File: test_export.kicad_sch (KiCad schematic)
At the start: 2 parts, among them U1 TestMCU

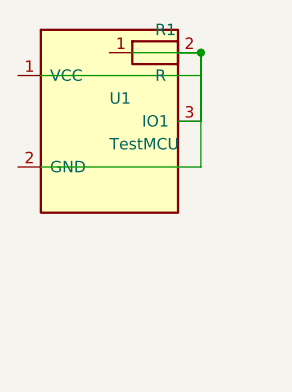
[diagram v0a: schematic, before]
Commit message: Fix duplicate reference designators, false positive PCB DRC clearance violations, and restore trace overlap resolution
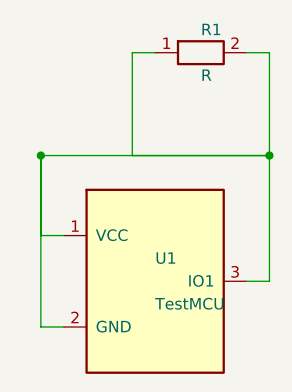
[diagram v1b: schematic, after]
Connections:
- net at R1.1: now also R1.2, U1.1 (VCC), U1.2 (GND), U1.3 (IO1)
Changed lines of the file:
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@@
 (kicad_sch (version 20231120) (generator "circuitbot") (generator_version "1.0")
   (paper "A3")
-  (symbol (lib_id "MCU_Module:TestMCU") (at 58.42 58.42 0) (unit 1)
+  (symbol (lib_id "MCU_Module:TestMCU") (at 63.5 76.2 0) (unit 1)
     (in_bom yes) (on_board yes) (dnp no)
-    (property "Reference" "U1" (at 58.42 55.88 0)
+    (property "Reference" "U1" (at 63.5 73.66 0)
       (effects (font (size 1.27 1.27)) (justify left))
     )
-    (property "Value" "TestMCU" (at 58.42 60.96 0)
+    (property "Value" "TestMCU" (at 63.5 78.74 0)
       (effects (font (size 1.27 1.27)) (justify left))
     )
-    (property "Footprint" "" (at 58.42 58.42 0)
+    (property "Footprint" "" (at 63.5 76.2 0)
       (effects (font (size 1.27 1.27)) hide)
     )
-    (property "Datasheet" "" (at 58.42 58.42 0)
+    (property "Datasheet" "" (at 63.5 76.2 0)
       (effects (font (size 1.27 1.27)) hide)
     )
@@
     (instances
       (project "circuitbot"
-        (path "/c2199af7-c479-45ad-89b1-c0f63471e519" (reference "U1") (unit 1))
+        (path "/90fcbd86-16bf-4343-8192-f2305b034c51" (reference "U1") (unit 1))
       )
     )
   )
-  (symbol (lib_id "Device:R") (at 63.5 50.8 0) (unit 1)
+  (symbol (lib_id "Device:R") (at 68.58 50.8 0) (unit 1)
     (in_bom yes) (on_board yes) (dnp no)
-    (property "Reference" "R1" (at 63.5 48.26 0)
+    (property "Reference" "R1" (at 68.58 48.26 0)
       (effects (font (size 1.27 1.27)) (justify left))
     )
-    (property "Value" "R" (at 63.5 53.34 0)
+    (property "Value" "R" (at 68.58 53.34 0)
       (effects (font (size 1.27 1.27)) (justify left))
     )
-    (property "Footprint" "" (at 63.5 50.8 0)
+    (property "Footprint" "" (at 68.58 50.8 0)
       (effects (font (size 1.27 1.27)) hide)
     )
-    (property "Datasheet" "" (at 63.5 50.8 0)
+    (property "Datasheet" "" (at 68.58 50.8 0)
       (effects (font (size 1.27 1.27)) hide)
     )
@@
     (instances
       (project "circuitbot"
-        (path "/c2199af7-c479-45ad-89b1-c0f63471e519" (reference "R1") (unit 1))
+        (path "/90fcbd86-16bf-4343-8192-f2305b034c51" (reference "R1") (unit 1))
       )
     )
   )
-  (wire (pts (xy 66.04 58.42) (xy 68.58 58.42))
+  (wire (pts (xy 73.66 76.2) (xy 76.2 76.2))
     (stroke (width 0) (type default))
   )
-  (wire (pts (xy 68.58 58.42) (xy 68.58 50.8))
+  (wire (pts (xy 76.2 76.2) (xy 76.2 62.23))
     (stroke (width 0) (type default))
   )
-  (wire (pts (xy 68.58 50.8) (xy 60.96 50.8))
+  (wire (pts (xy 76.2 62.23) (xy 60.96 62.23))
     (stroke (width 0) (type default))
   )
-  (wire (pts (xy 50.8 53.34) (xy 68.58 53.34))
+  (wire (pts (xy 60.96 62.23) (xy 60.96 50.8))
     (stroke (width 0) (type default))
   )
-  (wire (pts (xy 68.58 53.34) (xy 68.58 50.8))
+  (wire (pts (xy 60.96 50.8) (xy 63.5 50.8))
     (stroke (width 0) (type default))
   )
-  (wire (pts (xy 68.58 50.8) (xy 66.04 50.8))
+  (wire (pts (xy 53.34 71.12) (xy 50.8 71.12))
     (stroke (width 0) (type default))
   )
-  (wire (pts (xy 50.8 63.5) (xy 68.58 63.5))
+  (wire (pts (xy 50.8 71.12) (xy 50.8 62.23))
     (stroke (width 0) (type default))
   )
-  (wire (pts (xy 68.58 63.5) (xy 68.58 50.8))
+  (wire (pts (xy 50.8 62.23) (xy 76.2 62.23))
     (stroke (width 0) (type default))
   )
-  (junction (at 68.58 50.8) (diameter 0) (color 0 0 0 0)
+  (wire (pts (xy 76.2 62.23) (xy 76.2 50.8))
+    (stroke (width 0) (type default))
+  )
+  (wire (pts (xy 76.2 50.8) (xy 73.66 50.8))
+    (stroke (width 0) (type default))
+  )
+  (wire (pts (xy 53.34 81.28) (xy 50.8 81.28))
+    (stroke (width 0) (type default))
+  )
+  (wire (pts (xy 50.8 81.28) (xy 50.8 62.23))
+    (stroke (width 0) (type default))
+  )
+  (junction (at 76.2 62.23) (diameter 0) (color 0 0 0 0)
+  )
+  (junction (at 50.8 62.23) (diameter 0) (color 0 0 0 0)
   )
   (sheet_instances (path "/" (page "1")))

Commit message: Feat : Optimized the reRouting
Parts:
- removed R1: R, symbol Device:R
- removed U1: TestMCU, symbol MCU_Module:TestMCU
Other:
- title: (none) -> Smart USB Thumb Drive
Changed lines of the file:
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@@
 (kicad_sch (version 20231120) (generator "circuitbot") (generator_version "1.0")
   (paper "A3")
-  (symbol (lib_id "MCU_Module:TestMCU") (at 63.5 76.2 0) (unit 1)
-    (in_bom yes) (on_board yes) (dnp no)
-    (property "Reference" "U1" (at 63.5 73.66 0)
-      (effects (font (size 1.27 1.27)) (justify left))
-    )
-    (property "Value" "TestMCU" (at 63.5 78.74 0)
-      (effects (font (size 1.27 1.27)) (justify left))
-    )
-    (property "Footprint" "" (at 63.5 76.2 0)
-      (effects (font (size 1.27 1.27)) hide)
-    )
-    (property "Datasheet" "" (at 63.5 76.2 0)
-      (effects (font (size 1.27 1.27)) hide)
-    )
-    (pin "1")
-    (pin "2")
-    (pin "3")
-    (instances
-      (project "circuitbot"
-        (path "/90fcbd86-16bf-4343-8192-f2305b034c51" (reference "U1") (unit 1))
-      )
-    )
-  )
-  (symbol (lib_id "Device:R") (at 68.58 50.8 0) (unit 1)
-    (in_bom yes) (on_board yes) (dnp no)
-    (property "Reference" "R1" (at 68.58 48.26 0)
-      (effects (font (size 1.27 1.27)) (justify left))
-    )
-    (property "Value" "R" (at 68.58 53.34 0)
-      (effects (font (size 1.27 1.27)) (justify left))
-    )
-    (property "Footprint" "" (at 68.58 50.8 0)
-      (effects (font (size 1.27 1.27)) hide)
-    )
-    (property "Datasheet" "" (at 68.58 50.8 0)
-      (effects (font (size 1.27 1.27)) hide)
-    )
-    (pin "1")
-    (pin "2")
-    (instances
-      (project "circuitbot"
-        (path "/90fcbd86-16bf-4343-8192-f2305b034c51" (reference "R1") (unit 1))
-      )
-    )
-  )
-  (wire (pts (xy 73.66 76.2) (xy 76.2 76.2))
-    (stroke (width 0) (type default))
-  )
-  (wire (pts (xy 76.2 76.2) (xy 76.2 62.23))
-    (stroke (width 0) (type default))
-  )
-  (wire (pts (xy 76.2 62.23) (xy 60.96 62.23))
-    (stroke (width 0) (type default))
-  )
-  (wire (pts (xy 60.96 62.23) (xy 60.96 50.8))
-    (stroke (width 0) (type default))
-  )
-  (wire (pts (xy 60.96 50.8) (xy 63.5 50.8))
-    (stroke (width 0) (type default))
-  )
-  (wire (pts (xy 53.34 71.12) (xy 50.8 71.12))
-    (stroke (width 0) (type default))
-  )
-  (wire (pts (xy 50.8 71.12) (xy 50.8 62.23))
-    (stroke (width 0) (type default))
-  )
-  (wire (pts (xy 50.8 62.23) (xy 76.2 62.23))
-    (stroke (width 0) (type default))
-  )
-  (wire (pts (xy 76.2 62.23) (xy 76.2 50.8))
-    (stroke (width 0) (type default))
-  )
-  (wire (pts (xy 76.2 50.8) (xy 73.66 50.8))
-    (stroke (width 0) (type default))
-  )
-  (wire (pts (xy 53.34 81.28) (xy 50.8 81.28))
-    (stroke (width 0) (type default))
-  )
-  (wire (pts (xy 50.8 81.28) (xy 50.8 62.23))
-    (stroke (width 0) (type default))
-  )
-  (junction (at 76.2 62.23) (diameter 0) (color 0 0 0 0)
-  )
-  (junction (at 50.8 62.23) (diameter 0) (color 0 0 0 0)
+  (title_block
+    (title "Smart USB Thumb Drive")
+    (date "2026-06-21")
+    (rev "draft")
+    (source "generated by CircuitBot EDA agent")
   )
   (sheet_instances (path "/" (page "1")))

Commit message: Conversation UI overhaul: replace timeline with chat-style assistant messages and tool cards
- Replace emit_timeline_event() with emit_assistant_message() + emit_tool_event()
- All 9 node files converted to new conversation event types
- Frontend: timeline cards replaced by assistant bubbles + collapsible tool cards in unified conversation stream
- Remove old activityLog/agentLog split; single #agentConversation div
- Layout regression tests (8/8 passing) for blocks_v2 placement mode
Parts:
- added R1: R, symbol Device:R
- added U1: TestMCU, symbol MCU_Module:TestMCU
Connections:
- new net: R1.2, U1.1 (VCC)
- new net: R1.1, U1.3 (IO1)
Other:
- title: Smart USB Thumb Drive -> CircuitBot Generated Design
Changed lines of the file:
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@@
   (paper "A3")
   (title_block
-    (title "Smart USB Thumb Drive")
-    (date "2026-06-21")
+    (title "CircuitBot Generated Design")
+    (date "2026-06-23")
     (rev "draft")
-    (source "generated by CircuitBot EDA agent")
+    (company "")
+    (comment 1 "generated by CircuitBot EDA agent")
   )
+  (symbol (lib_id "MCU_Module:TestMCU") (at 63.5 76.2 0) (unit 1)
+    (body_style 1)
+    (exclude_from_sim no)
+    (in_bom yes) (on_board yes) (in_pos_files yes) (dnp no)
+    (property "Reference" "U1" (at 63.5 73.66 0)
+      (effects (font (size 1.27 1.27)) (justify left))
+    )
+    (property "Value" "TestMCU" (at 63.5 78.74 0)
+      (effects (font (size 1.27 1.27)) (justify left))
+    )
+    (property "Footprint" "" (at 63.5 76.2 0)
+      (effects (font (size 1.27 1.27)) hide)
+    )
+    (property "Datasheet" "" (at 63.5 76.2 0)
+      (effects (font (size 1.27 1.27)) hide)
+    )
+    (pin "1")
+    (pin "2")
+    (pin "3")
+    (instances
+      (project "circuitbot"
+        (path "/b2903a28-125e-4906-bfcd-02d244d2eb6a" (reference "U1") (unit 1))
+      )
+    )
+  )
+  (symbol (lib_id "Device:R") (at 68.58 50.8 0) (unit 1)
+    (body_style 1)
+    (exclude_from_sim no)
+    (in_bom yes) (on_board yes) (in_pos_files yes) (dnp no)
+    (property "Reference" "R1" (at 68.58 48.26 0)
+      (effects (font (size 1.27 1.27)) (justify left))
+    )
+    (property "Value" "R" (at 68.58 53.34 0)
+      (effects (font (size 1.27 1.27)) (justify left))
+    )
+    (property "Footprint" "" (at 68.58 50.8 0)
+      (effects (font (size 1.27 1.27)) hide)
+    )
+    (property "Datasheet" "" (at 68.58 50.8 0)
+      (effects (font (size 1.27 1.27)) hide)
+    )
+    (pin "1")
+    (pin "2")
+    (instances
+      (project "circuitbot"
+        (path "/b2903a28-125e-4906-bfcd-02d244d2eb6a" (reference "R1") (unit 1))
+      )
+    )
+  )
+  (wire (pts (xy 73.66 76.2) (xy 76.2 76.2))
+    (stroke (width 0) (type default))
+  )
+  (wire (pts (xy 76.2 76.2) (xy 76.2 62.23))
+    (stroke (width 0) (type default))
+  )
+  (wire (pts (xy 76.2 62.23) (xy 60.96 62.23))
+    (stroke (width 0) (type default))
+  )
+  (wire (pts (xy 60.96 62.23) (xy 60.96 50.8))
+    (stroke (width 0) (type default))
+  )
+  (wire (pts (xy 60.96 50.8) (xy 63.5 50.8))
+    (stroke (width 0) (type default))
+  )
+  (wire (pts (xy 53.34 71.12) (xy 50.8 71.12))
+    (stroke (width 0) (type default))
+  )
+  (wire (pts (xy 50.8 71.12) (xy 50.8 55.88))
+    (stroke (width 0) (type default))
+  )
+  (wire (pts (xy 50.8 55.88) (xy 76.2 55.88))
+    (stroke (width 0) (type default))
+  )
+  (wire (pts (xy 76.2 55.88) (xy 76.2 50.8))
+    (stroke (width 0) (type default))
+  )
+  (wire (pts (xy 76.2 50.8) (xy 73.66 50.8))
+    (stroke (width 0) (type default))
+  )
+  # WARNING: possible accidental short at (76.2, 76.2) — 2 wire segments meet at non-pin coordinate
+  # WARNING: possible accidental short at (76.2, 62.23) — 2 wire segments meet at non-pin coordinate
+  # WARNING: possible accidental short at (60.96, 62.23) — 2 wire segments meet at non-pin coordinate
+  # WARNING: possible accidental short at (60.96, 50.8) — 2 wire segments meet at non-pin coordinate
+  # WARNING: possible accidental short at (50.8, 71.12) — 2 wire segments meet at non-pin coordinate
+  # WARNING: possible accidental short at (50.8, 55.88) — 2 wire segments meet at non-pin coordinate
+  # WARNING: possible accidental short at (76.2, 55.88) — 2 wire segments meet at non-pin coordinate
+  # WARNING: possible accidental short at (76.2, 50.8) — 2 wire segments meet at non-pin coordinate
+  # ⚠ KiCad export: 8 potential accidental short(s) detected — review wire vertices at the coordinates above
   (sheet_instances (path "/" (page "1")))
 )

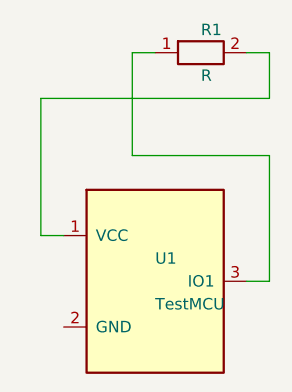
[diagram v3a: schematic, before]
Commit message: Overhaul: subprocess pcbnew, human approval gate, ERC auto-fix with wire_paths check, centroid power fan-out
- pcbnew runs as subprocess (KiCad's python.exe), not sys.path injection
- Human approval gate between schematic and PCB with SocketIO buttons
- ERC auto-fix checks wire_paths (actual traces) not netlist (abstract connections)
- Stale netlist connections removed before re-wiring in routing node
- MAX_WIRE_LEN 300mm on ERC re-routing passes (was 150mm)
- Centroid hub for power-net fan-out instead of sort-by-Y
- PWR_FLAG injection includes GND nets
- Orphan-rescued power pins merged via _merge_net
- Signal-pin filter: pin_not_connected for unassigned pins skipped in ERC loop
- PCB_IO.Load() for KiCad 10.0 compatibility
- SHIELD pin auto-assigned to GND net
- Debug prints removed from schematic_repair and schematic_audit
- Routing topology: _find_attachment_buddy with power_pins fallback
- Layout engine: MAX_COLLISIONS 2->5, MAX_WIRE_MANHATTAN 150->200
- S-expression power-net fan-out with centroid hub, no orphan labels
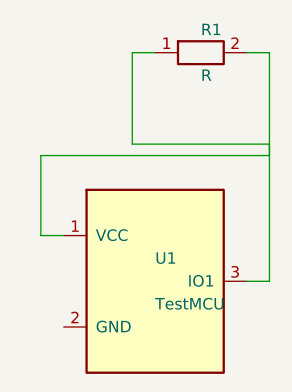
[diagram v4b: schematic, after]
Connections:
- net at R1.2, U1.1 (VCC): now also R1.1, U1.3 (IO1)
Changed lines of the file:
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@@
   (title_block
     (title "CircuitBot Generated Design")
-    (date "2026-06-23")
+    (date "2026-06-25")
     (rev "draft")
     (company "")
@@
     (instances
       (project "circuitbot"
-        (path "/b2903a28-125e-4906-bfcd-02d244d2eb6a" (reference "U1") (unit 1))
+        (path "/89608b8e-64a7-433a-a97b-f3e192fc43a3" (reference "U1") (unit 1))
       )
     )
@@
     (instances
       (project "circuitbot"
-        (path "/b2903a28-125e-4906-bfcd-02d244d2eb6a" (reference "R1") (unit 1))
+        (path "/89608b8e-64a7-433a-a97b-f3e192fc43a3" (reference "R1") (unit 1))
       )
     )
@@
     (stroke (width 0) (type default))
   )
-  (wire (pts (xy 76.2 76.2) (xy 76.2 62.23))
+  (wire (pts (xy 76.2 76.2) (xy 76.2 60.96))
     (stroke (width 0) (type default))
   )
-  (wire (pts (xy 76.2 62.23) (xy 60.96 62.23))
+  (wire (pts (xy 76.2 60.96) (xy 60.96 60.96))
     (stroke (width 0) (type default))
   )
-  (wire (pts (xy 60.96 62.23) (xy 60.96 50.8))
+  (wire (pts (xy 60.96 60.96) (xy 60.96 50.8))
     (stroke (width 0) (type default))
   )
@@
     (stroke (width 0) (type default))
   )
-  (wire (pts (xy 50.8 71.12) (xy 50.8 55.88))
+  (wire (pts (xy 50.8 71.12) (xy 50.8 62.23))
     (stroke (width 0) (type default))
   )
-  (wire (pts (xy 50.8 55.88) (xy 76.2 55.88))
+  (wire (pts (xy 50.8 62.23) (xy 76.2 62.23))
     (stroke (width 0) (type default))
   )
-  (wire (pts (xy 76.2 55.88) (xy 76.2 50.8))
+  (wire (pts (xy 76.2 62.23) (xy 76.2 50.8))
     (stroke (width 0) (type default))
   )
@@
   )
   # WARNING: possible accidental short at (76.2, 76.2) — 2 wire segments meet at non-pin coordinate
-  # WARNING: possible accidental short at (76.2, 62.23) — 2 wire segments meet at non-pin coordinate
-  # WARNING: possible accidental short at (60.96, 62.23) — 2 wire segments meet at non-pin coordinate
+  # WARNING: possible accidental short at (76.2, 60.96) — 2 wire segments meet at non-pin coordinate
+  # WARNING: possible accidental short at (60.96, 60.96) — 2 wire segments meet at non-pin coordinate
   # WARNING: possible accidental short at (60.96, 50.8) — 2 wire segments meet at non-pin coordinate
   # WARNING: possible accidental short at (50.8, 71.12) — 2 wire segments meet at non-pin coordinate
-  # WARNING: possible accidental short at (50.8, 55.88) — 2 wire segments meet at non-pin coordinate
-  # WARNING: possible accidental short at (76.2, 55.88) — 2 wire segments meet at non-pin coordinate
+  # WARNING: possible accidental short at (50.8, 62.23) — 2 wire segments meet at non-pin coordinate
+  # WARNING: possible accidental short at (76.2, 62.23) — 2 wire segments meet at non-pin coordinate
   # WARNING: possible accidental short at (76.2, 50.8) — 2 wire segments meet at non-pin coordinate
   # ⚠ KiCad export: 8 potential accidental short(s) detected — review wire vertices at the coordinates above
